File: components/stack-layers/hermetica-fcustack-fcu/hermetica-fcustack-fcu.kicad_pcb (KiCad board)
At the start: 4 copper layers, 70.5 x 50.8 mm, 114 parts, among them IC1 SN74LVC1G14-Q1, J1 Conn_02x50_Odd_Even, J2 JANOS-STACK-DEBUG-V1, J3 Conn_02x50_Odd_Even, Q1 NPN, Q4 NEXPERIA-BSS138-SOT-23-3, Q5 DDTC114EE-7-F, Q6 DIODESINC-MMBT4401-7-F-SOT-23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, U1 74AHC1G17GWH, U10 74AHC1G17GWH, U11 74AHC1G17GWH, U12 74AHC1G17GWH, U13 74AUC1G08, U14 74AHCT1G32, U15 74AHC1G17GWH, U16 74AHCT121A, U17 74AHC1G17GWH, U18 PESD2CANFD24V-QCZ, U2 74AHC1G17GWH, U21 PESD2CANFD24V-QCZ, U3 74AHC1G17GWH, U4 LM66100DCK, U5 LM66100DCK, U6 74AHC1G17GWH, U7 MB85RS1MT, U8 LP5912-3.3DRV, U9 LM66100DCK, Y1 ABRACON-ABM10AIG-48.000MHZ-4Z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

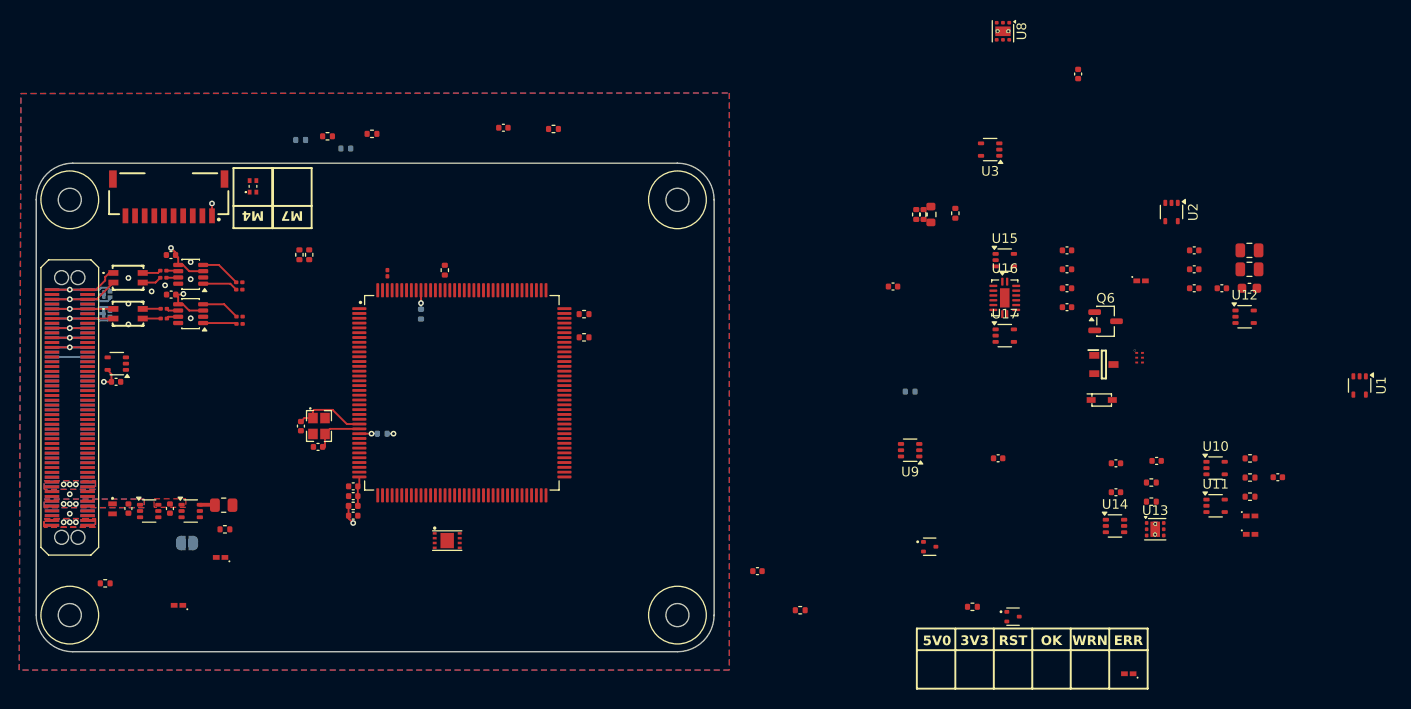
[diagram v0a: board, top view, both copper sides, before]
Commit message: STM32H755ZIT6 dev board
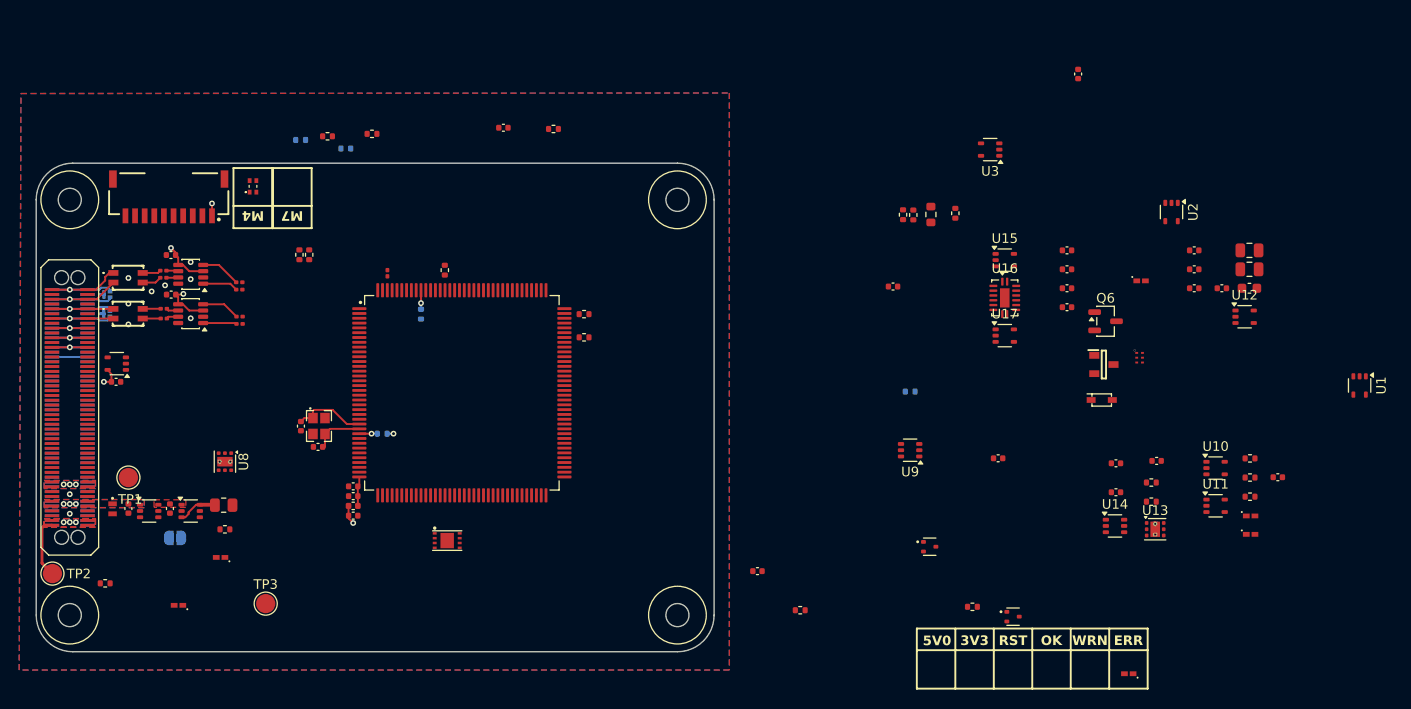
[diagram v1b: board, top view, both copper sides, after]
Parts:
- added TP1: TestPoint, TestPoint:TestPoint_Pad_D2.0mm, F.Cu at (-25.7, 7.29)
- added TP2: TestPoint, TestPoint:TestPoint_Pad_D2.0mm, F.Cu at (-33.6, 17.3)
- added TP3: TestPoint, TestPoint:TestPoint_Pad_D2.0mm, F.Cu at (-11.4, 20.4)
- moved U8 92.5 mm to (-15.6, 5.64)
- moved R20 1.37 mm to (54.9, -20.0)
- moved JP1 1.35 mm to (-20.8, 13.6)
- moved R22 1.07 mm to (56.0, -20.0)
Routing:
- net /backplane/BP_VBAT_2A: track 0.00 -> 9.21 mm
- net /backplane/5V_MON+: track 1.52 -> 4.06 mm
